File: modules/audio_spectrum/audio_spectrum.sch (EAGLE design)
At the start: 64 parts, among them J1 MODULE_GENERIC, J2 AUDIO-JACK-VERTICAL, J7 TC2030-JLINK-L, P1 4k-200k, P2 4k-200k, Q1 NX3008PBK, Q2 NX3008PBK, U1 SAM4LC8AA, U2 MSGEQ7, U3 MSGEQ7, U5 OPA344, U6 OPA344, U7 TLV62130, X2 16MHz

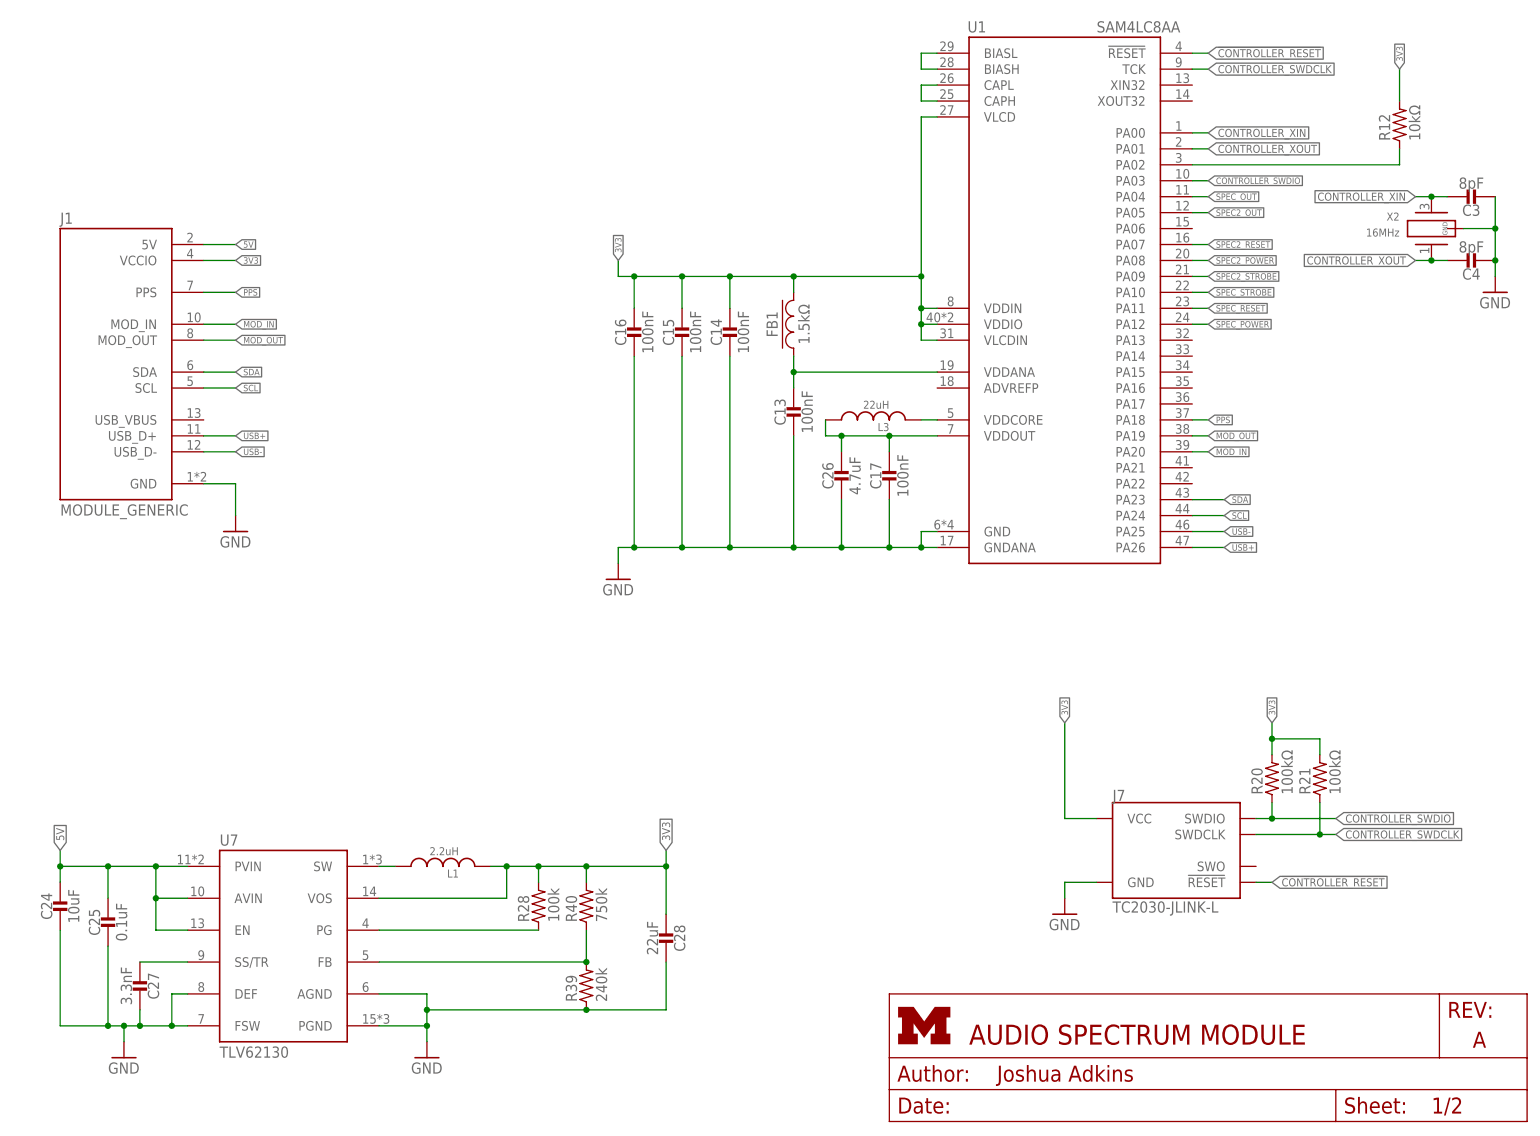
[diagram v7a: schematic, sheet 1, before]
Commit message: ran pats script, added a four LEDs
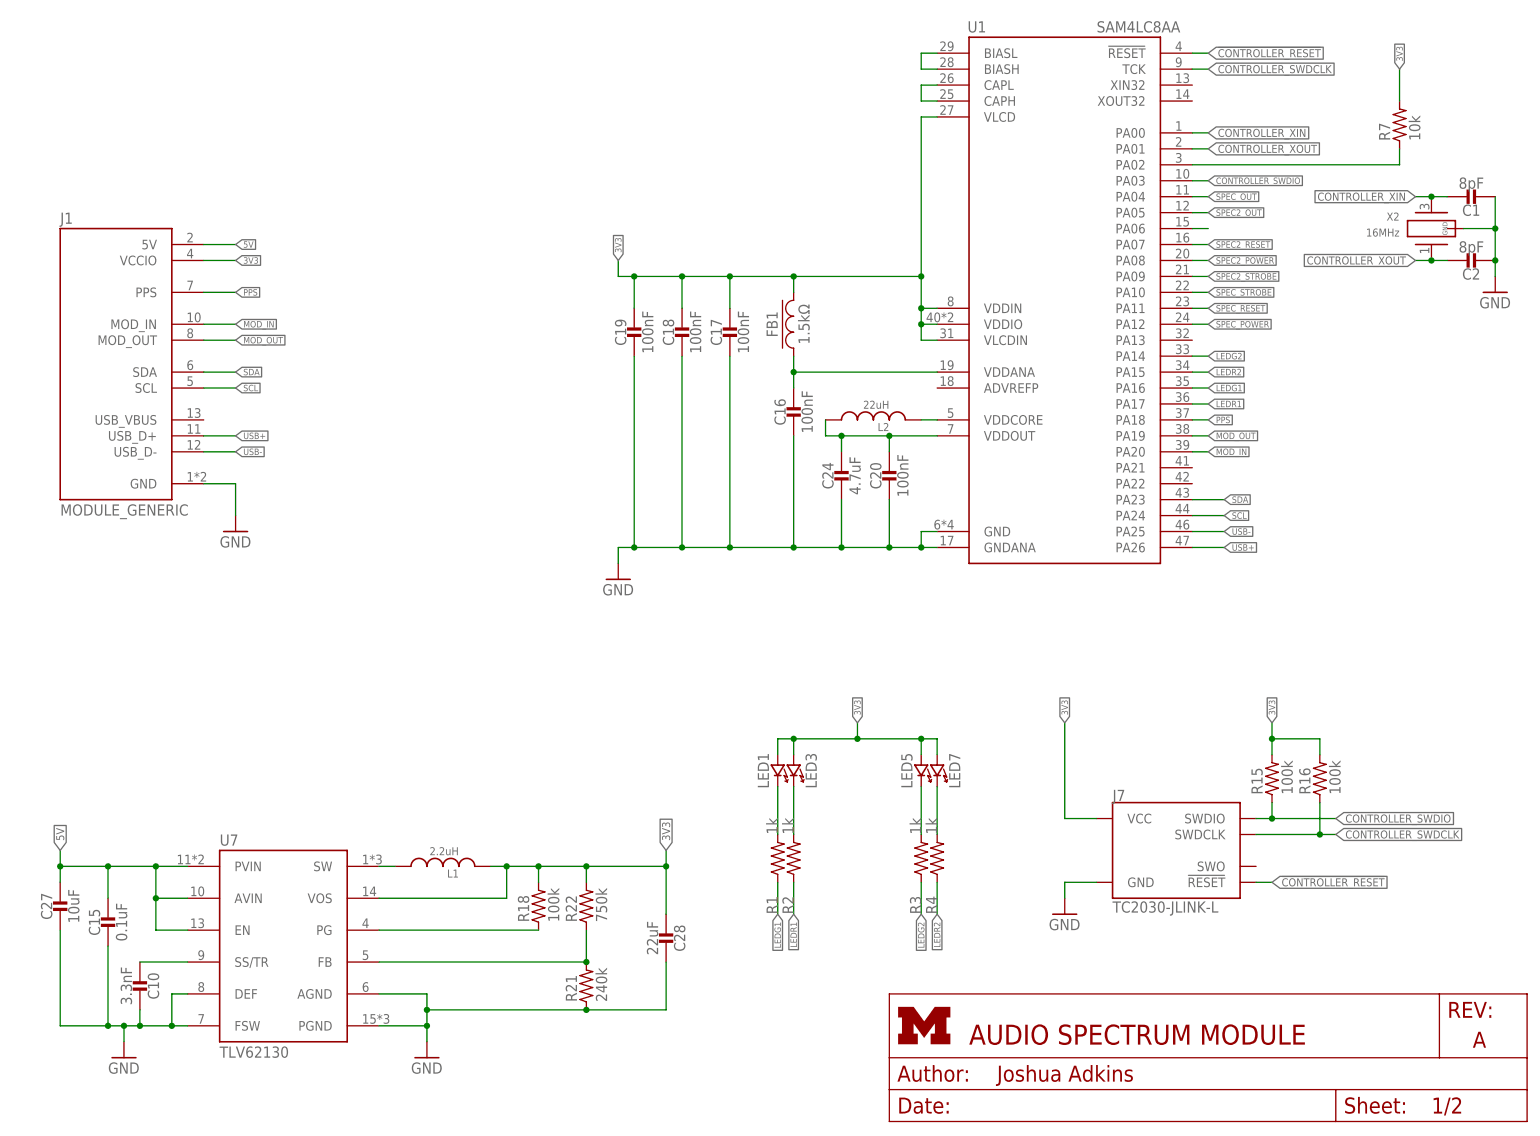
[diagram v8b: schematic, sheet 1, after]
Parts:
- removed R39: 240k, passives:RESISTOR0603_RES
- added LED1, LED3, LED5, LED7: LED0603, leds:LED0603
- added R13: 20k, passives:RESISTOR0603_RES
- added R16, R17: 100k, passives:RESISTOR0603_RES
- added R19: 200k, passives:RESISTOR0603_RES
- added R9: 10k, passives:RESISTOR0603_RES
- C1: value 0.1uF -> 8pF; DIGIKEY (none) -> 490-8230-1-ND
- C10: value 1nF -> 3.3nF
- C11: value 1uF -> 0.1uF
- C12: value 100pF -> 0.1uF
- C13, C14, C15: value 100nF -> 0.1uF; DIGIKEY 490-10777-1-ND -> (none)
- C18: value 4.7uF -> 100nF; DIGIKEY (none) -> 490-10777-1-ND
- C19: value 1uF -> 100nF; DIGIKEY (none) -> 490-10777-1-ND
- C2: value 33pF -> 8pF; DIGIKEY (none) -> 490-8230-1-ND
- C20: value 100pF -> 100nF; DIGIKEY (none) -> 490-10777-1-ND
- C21: value 4.7uF -> 1uF
- C23: value 1nF -> 1uF
- C24: value 10uF -> 4.7uF; DIGIKEY (none) -> 490-13252-1-ND
- C25: value 0.1uF -> 4.7uF
- C26: DIGIKEY 490-13252-1-ND -> (none)
- C27: value 3.3nF -> 10uF
- C3, C4: value 8pF -> 33pF; DIGIKEY 490-8230-1-ND -> (none)
- C5, C6: value 0.1uF -> 100pF
- C7: value 33pF -> 1nF
- C9: value 0.1uF -> 1nF
- R1, R2, R3, R4: value 20k -> 1k; DIGIKEY (none) -> 1276-3431-1-ND
- R10: value 100k -> 20k
- R11: value 1.5k -> 20k
- R12: value 10kΩ -> 20k; DIGIKEY 1276-3431-1-ND -> (none)
- R14: value 10k -> 60k
- R15: value 10k -> 100k; DIGIKEY (none) -> 1276-3432-1-ND
- R20: value 100kΩ -> 200k; DIGIKEY 1276-3432-1-ND -> (none)
- R21: value 100kΩ -> 240k; DIGIKEY 1276-3432-1-ND -> (none)
- R5, R6: value 200k -> 1.5k
- R7: value 60k -> 10k; DIGIKEY (none) -> 1276-3431-1-ND
- R8: value 1.5k -> 10k
- renumbered L3 to L2, R28 to R18, R40 to R22
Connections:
- new net LEDG1: R1.1, U1.PA16
- new net LEDG2: R3.1, U1.PA14
- new net LEDR1: R2.1, U1.PA17
- new net LEDR2: R4.1, U1.PA15
- new net N$21: LED1.CATHODE, R1.2
- new net N$23: LED3.CATHODE, R2.2
- new net N$25: LED7.CATHODE, R4.2
- new net N$31: U1.PA06
- new net N$33: LED5.CATHODE, R3.2
- net 3V3: now also C17.1, C18.1, C19.1, LED1.ANODE, LED3.ANODE, LED5.ANODE, LED7.ANODE, R15.2, R16.2, R7.2; no longer C14.1, C15.1, C16.1, R12.2, R20.2, R21.2
- net 5V: now also C15.1, C27.1; no longer C24.1, C25.1
- net CONTROLLER_BUCK/LDO_N: now also R7.1; no longer R12.1
- net CONTROLLER_SWDCLK: now also R16.1; no longer R21.1
- net CONTROLLER_SWDIO: now also R15.1; no longer R20.1
- net CONTROLLER_XIN: now also C1.1; no longer C3.1
- net CONTROLLER_XOUT: now also C2.1; no longer C4.1
- net GND: now also C10.1, C11.2, C12.2, C18.2, C19.2, C20.2, C21.1, C27.2, C9.1, R11.2, R13.2, R21.1; no longer C11.1, C19.1, C25.2, C26.2, C27.1, C5.2, C6.2, C7.2, C9.2, R2.2, R39.1, R4.2
- net N$1: now also C11.1; no longer C1.1
- net N$10: now also C26.2, R8.2, R9.2; no longer C21.2, R14.2, R15.2
- net N$11: now also C22.2, R12.2, R13.1; no longer C19.2, R1.2, R2.1
- net N$12: now also C5.2, R14.1, R5.2; no longer C12.2, R7.1, R8.2
- net N$13: now also C25.1, R5.1; no longer C18.1, R8.1
- net N$14: now also C6.2, R17.1, R6.2; no longer C20.2, R10.1, R11.2
- net N$15: now also C26.1, R6.1; no longer C21.1, R11.1
- net N$16: now also R9.1; no longer R15.1
- net N$17: now also R8.1; no longer R14.1
- net N$18: now also C25.2; no longer C18.2
- net N$2: now also C3.1, R19.2; no longer C2.1, R5.2
- net N$3: now also C7.1; no longer C8.1
- net N$32: now also C16.1; no longer C13.1
- net N$34: now also C10.2; no longer C27.2
- net N$37: now also R21.2; no longer R39.2
- net N$4: now also C6.1, C7.2, R17.2; no longer C20.1, C8.2, R10.2
- net N$44: now also C20.1, C24.1; no longer C17.1, C26.1
- net N$5: now also C13.1; no longer C6.1
- net N$6: now also C4.1, R20.2; no longer C7.1, R6.2
- net N$7: now also C8.1; no longer C10.1
- net N$8: now also C5.1, C8.2, R14.2; no longer C10.2, C12.1, R7.2
- net N$9: now also C21.2, R10.2, R11.1; no longer C11.2, R3.2, R4.1
- net SPEC2_GATED: now also C12.1, R12.1, R19.1; no longer C5.1, R1.1, R5.1
- net SPEC_GATED: now also C14.1, C9.2, R10.1, R20.1; no longer C22.2, C9.1, R3.1, R6.1
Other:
- moved on the sheet: C11, C12, C15, C16, C17, C21, C22, C23, C24, C27, C5, C6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
